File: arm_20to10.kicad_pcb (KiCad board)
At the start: 2 copper layers, 16.9 x 29.7 mm, 10 parts, among them J1 SFH11-PBPC-D10-RA-BK, J2 20021111-00010T4LF, SW1 SSSS810701, U1 MIC5504-3.3YM5 TR

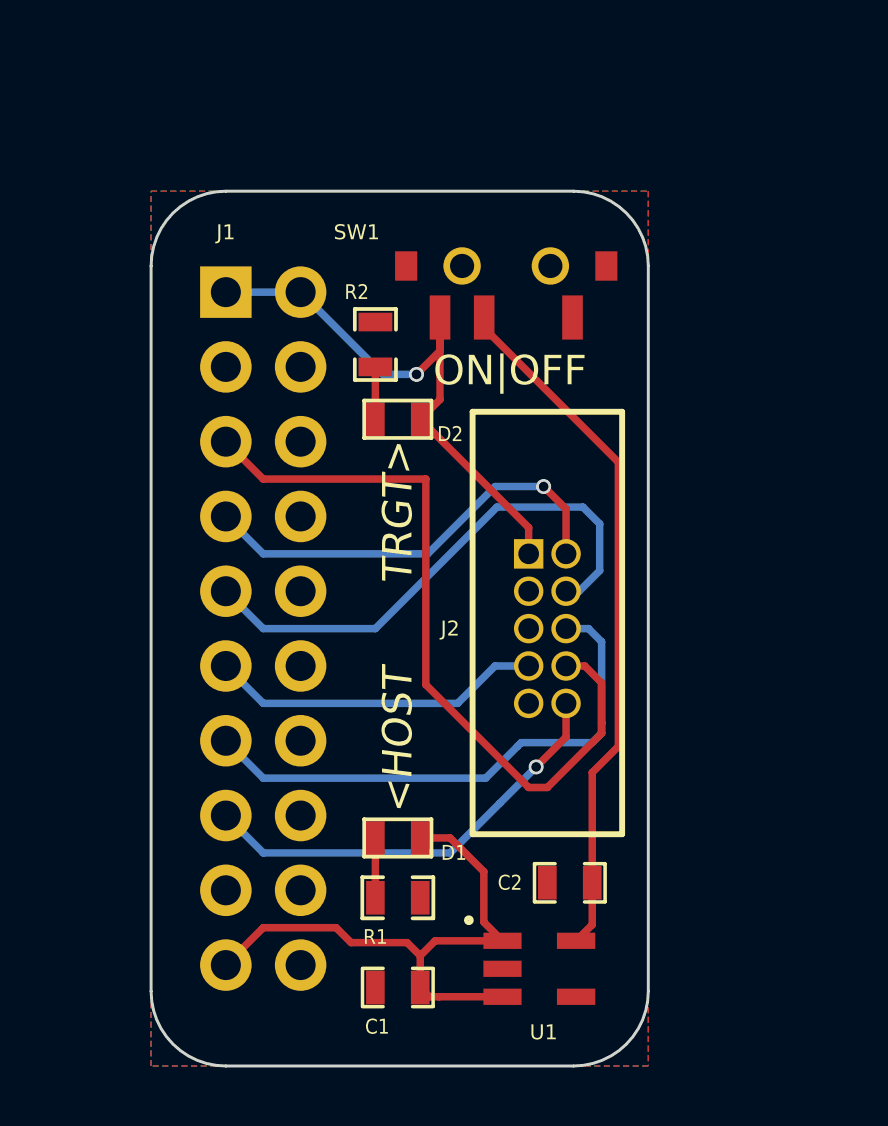
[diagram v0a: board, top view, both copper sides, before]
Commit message: - update with new arm 20 pin TH pinout - rework silks a bit to be more readable - add silk url to the back
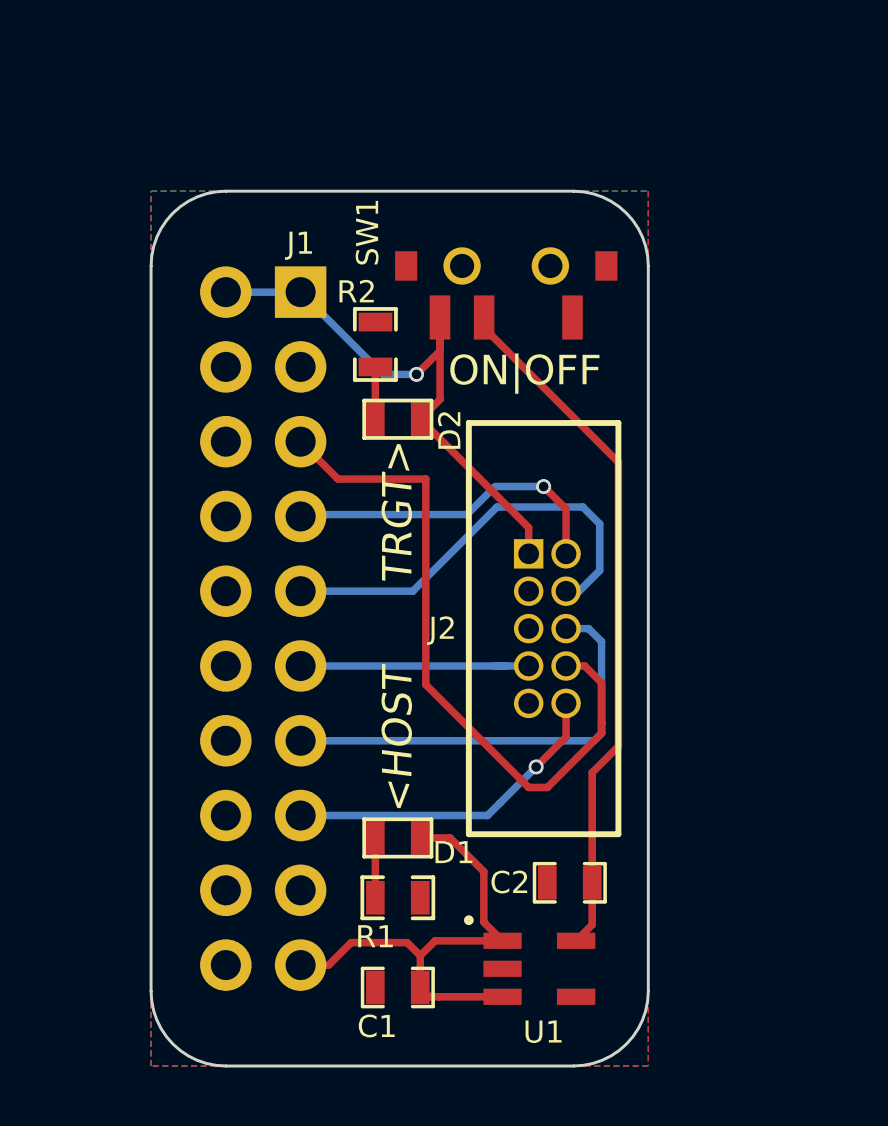
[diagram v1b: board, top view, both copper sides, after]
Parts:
- moved J1 2.54 mm to (202.6, 154.9)
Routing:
- net /TMS/SWDIO: track 14.9 -> 11.3 mm
- net /NRST: track 14.9 -> 11.3 mm
- net /TCLK/SWCLK: track 18.2 -> 14.6 mm
- net /SWO/TDO: track 18.5 -> 14.9 mm
- net /RTCK: track 11.3 -> 8.13 mm
- net /5V: track 19.8 -> 16.8 mm
- net /TDI: track 25.6 -> 23.1 mm
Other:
- board text added: "github.com/noahp/arm_20to10 v2.0"

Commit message: try to add some models
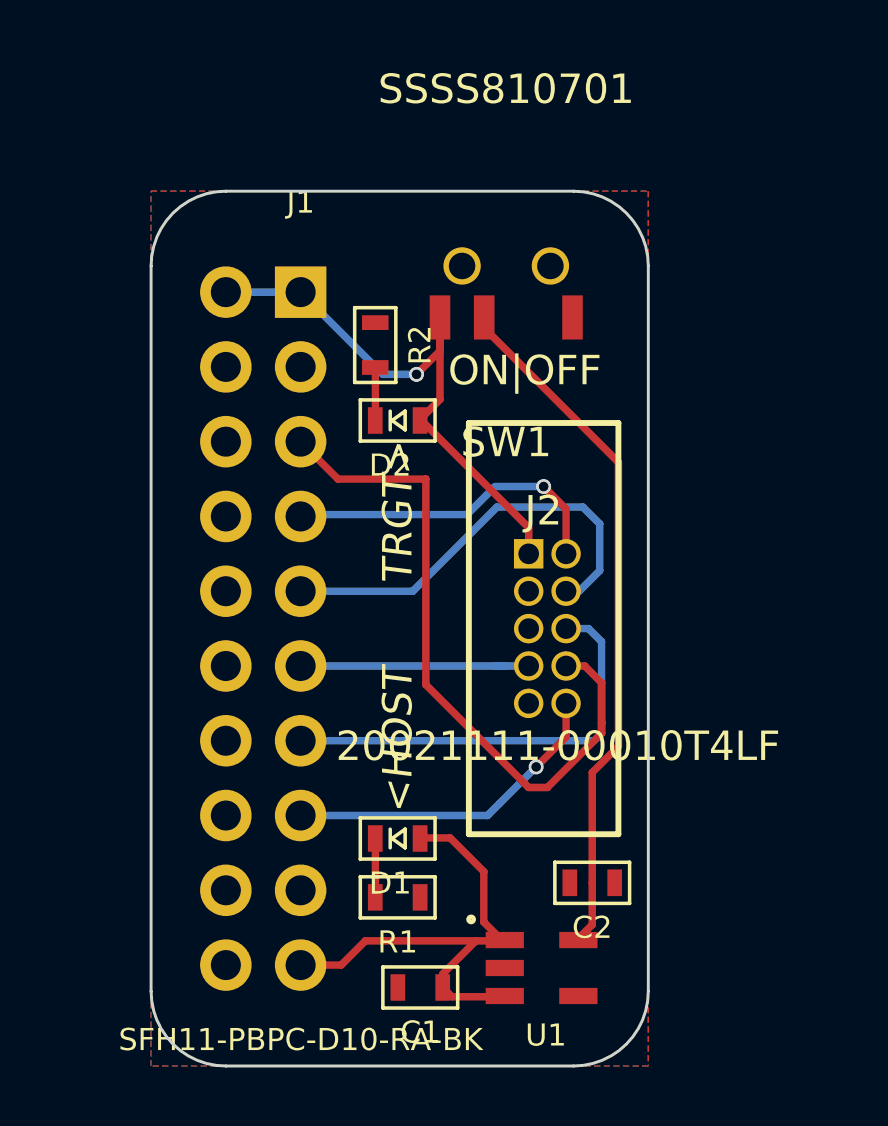
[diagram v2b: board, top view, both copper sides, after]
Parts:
- C1, C2: footprint SMD_Packages:SMD-0603_c -> kicadlib:SMD_0603_C
- D1, D2: footprint SMD_Packages:SMD-0603 -> kicadlib:SMD_0603_LED
- R1, R2: footprint SMD_Packages:SMD-0603_r -> kicadlib:SMD_0603_R
- moved R2 0.78 mm to (205.1, 157.5)
- moved D2 0.77 mm to (205.1, 159.3)
- moved D1 0.77 mm to (205.1, 173.5)
- moved R1 0.77 mm to (205.1, 175.5)
- moved U1 0.08 mm to (209.5, 177.9)
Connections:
- C2 pad 2: GND -> Net-(C2-Pad2)
- SW1 pad 2: Net-(C2-Pad1) -> Net-(SW1-Pad2)
- U1 pad 5: Net-(C2-Pad1) -> Net-(SW1-Pad2)
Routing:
- net Net-(SW1-Pad2): track 0.00 -> 23.7 mm
- net Net-(C2-Pad1): track 23.7 -> 0.00 mm
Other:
- board text added: "github.com/noahp/arm_20to10 v2.1"
- board text removed: "github.com/noahp/arm_20to10 v2.0"
